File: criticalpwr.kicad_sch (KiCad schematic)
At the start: 6 parts, among them J3 Power Conn

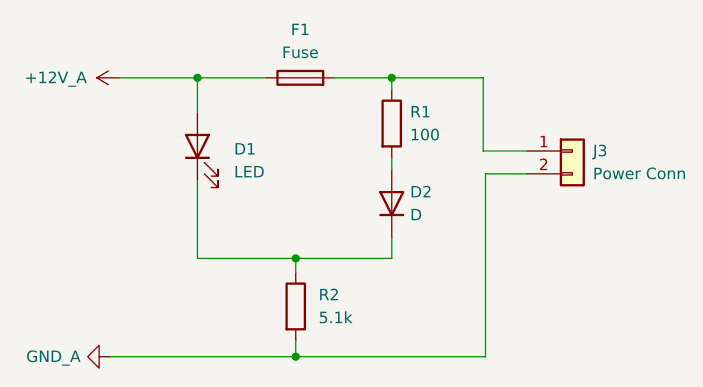
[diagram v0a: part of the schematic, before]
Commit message: removed LEDs
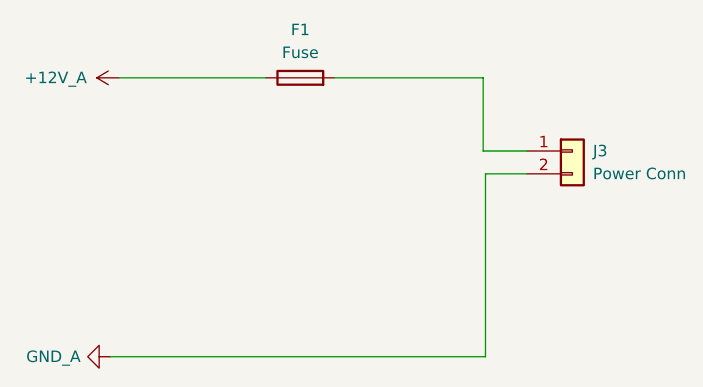
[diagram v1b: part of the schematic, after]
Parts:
- removed D1: LED, symbol Device:LED
- removed D2: D, symbol Device:D
- removed R1: 100, symbol Device:R
- removed R2: 5.1k, symbol Device:R

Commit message: finished schematic
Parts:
- added D1, D2, D20, D3, D4, D5, D6: 20mA, LED_SMD:LED_0805_2012Metric, symbol Device:LED
- added F22, F4, F5, F6, F7, F8: 10A, footprints:3588, symbol Device:Fuse
- added J10, J22, J6, J7, J8, J9: CRIT OUT, footprints:Molex_Micro-Fit_3.0_43650-0215_1x02_P3.00mm_Vertical, symbol Connector_Generic:Conn_01x02
- added R1, R2, R20, R3, R4, R5, R6: 505, Resistor_SMD:R_0805_2012Metric, symbol Device:R
- F1: value Fuse -> 10A
- J3: value Power Conn -> CRIT OUT
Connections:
- net at F1.2, J3.1 (Pin_1): now also R1.1
- net +12V_A renamed +12V_CRIT
- net +12V_CRIT: now also F22.1, F4.1, F5.1, F6.1, F7.1, F8.1
- net GND_A renamed GND
- net GND: now also D1.1 (K), D2.1 (K), D20.1 (K), D3.1 (K), D4.1 (K), D5.1 (K), D6.1 (K), J10.2 (Pin_2), J22.2 (Pin_2), J6.2 (Pin_2), J7.2 (Pin_2), J8.2 (Pin_2), J9.2 (Pin_2)
- new net: F5.2, J7.1 (Pin_1), R3.1
- new net: F4.2, J6.1 (Pin_1), R2.1
- new net: D6.2 (A), R6.2
- new net: F22.2, J22.1 (Pin_1), R20.1
- new net: D20.2 (A), R20.2
- new net: D1.2 (A), R1.2
- new net: F8.2, J10.1 (Pin_1), R6.1
- new net: D2.2 (A), R2.2
- new net: D4.2 (A), R4.2
- new net: F6.2, J8.1 (Pin_1), R4.1
- new net: F7.2, J9.1 (Pin_1), R5.1
- new net: D5.2 (A), R5.2
- new net: D3.2 (A), R3.2

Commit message: finished pcb
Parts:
- R1, R2, R20, R3, R4, R5, R6: value 505 -> 1k
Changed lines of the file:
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@@
 			)
 		)
-		(property "Value" "505"
+		(property "Value" "1k"
 			(at 58.42 32.766 90)
 			(effects
@@
 			)
 		)
-		(property "Value" "505"
+		(property "Value" "1k"
 			(at 119.38 94.996 90)
 			(effects
@@
 			)
 		)
-		(property "Value" "505"
+		(property "Value" "1k"
 			(at 58.42 94.996 90)
 			(effects
@@
 			)
 		)
-		(property "Value" "505"
+		(property "Value" "1k"
 			(at 119.38 32.766 90)
 			(effects
@@
 			)
 		)
-		(property "Value" "505"
+		(property "Value" "1k"
 			(at 58.42 63.246 90)
 			(effects
@@
 			)
 		)
-		(property "Value" "505"
+		(property "Value" "1k"
 			(at 119.38 63.246 90)
 			(effects
@@
 			)
 		)
-		(property "Value" "505"
+		(property "Value" "1k"
 			(at 58.42 128.016 90)
 			(effects

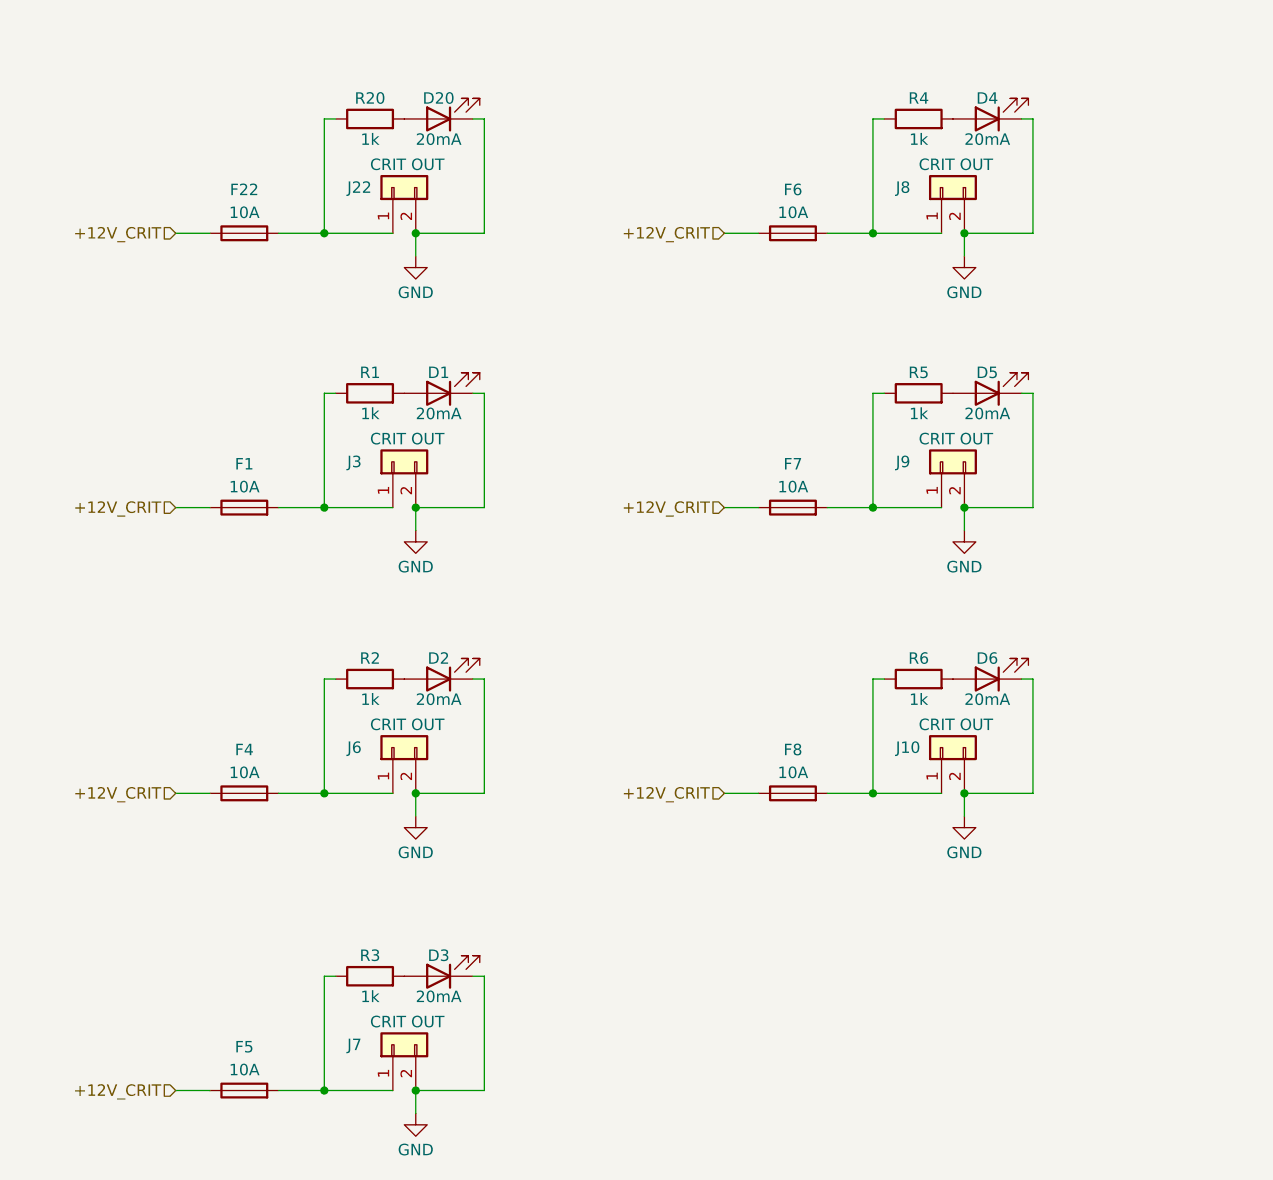
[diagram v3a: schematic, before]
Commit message: rearranged fuses on the back and and connectors on the front for improved waterproofing
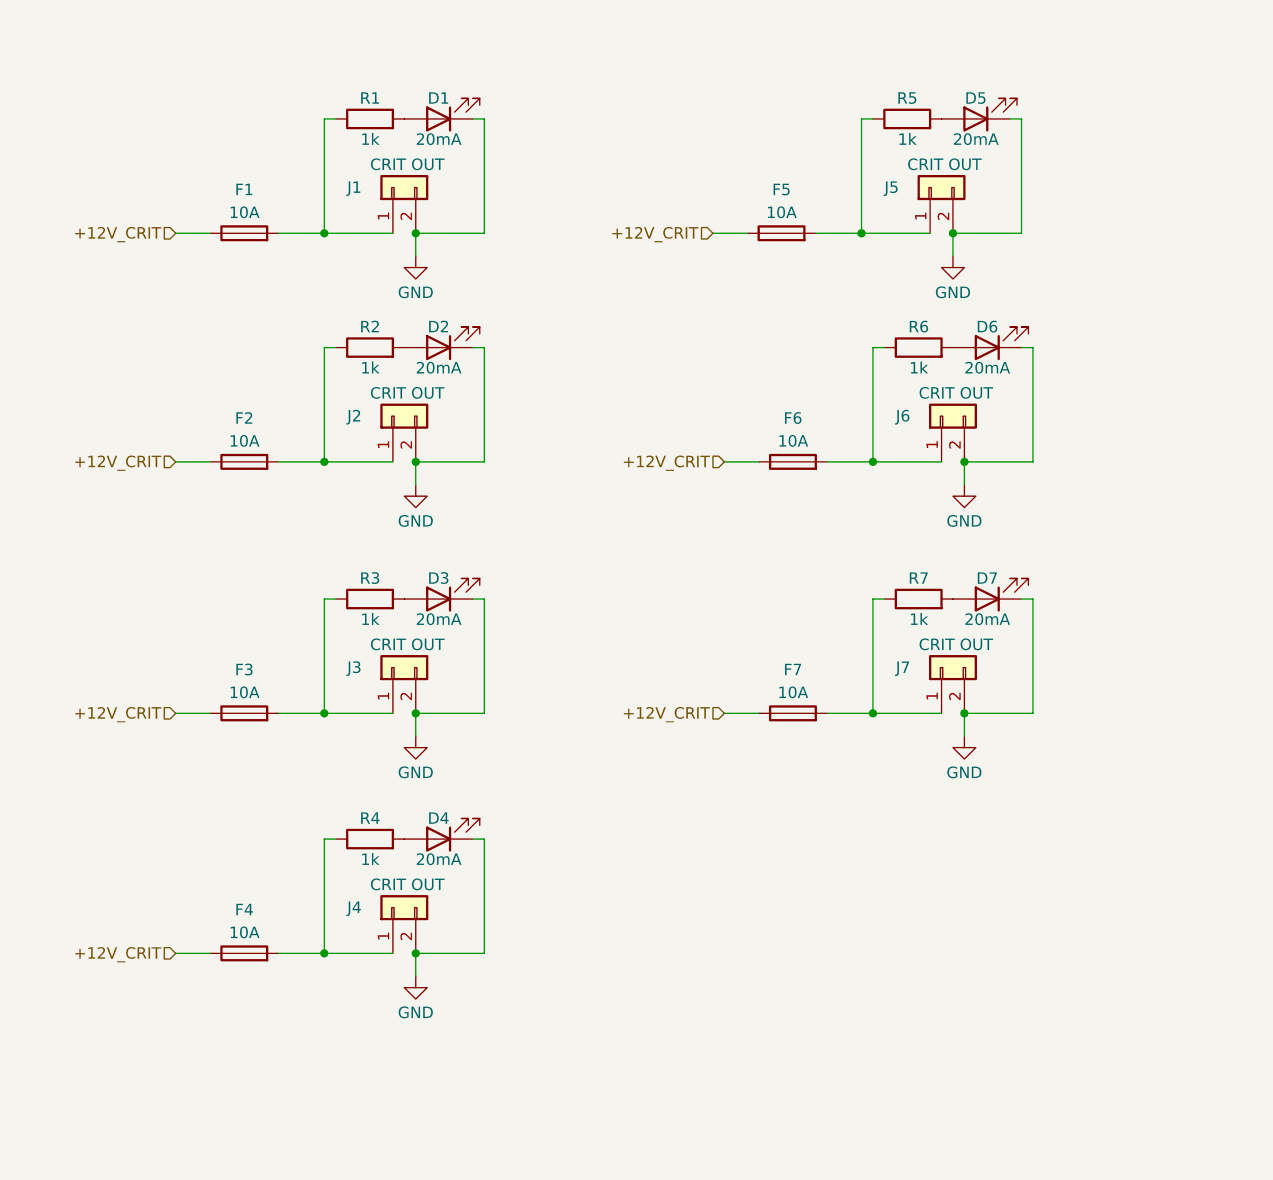
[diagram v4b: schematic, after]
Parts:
- renumbered D20 to D1, D6 to D2, D5 to D3, D3 to D5, D2 to D6, D1 to D7, F22 to F1, F8 to F2, F7 to F3, F6 to F4, F4 to F6, F1 to F7, J22 to J1, J10 to J2, J9 to J3, J8 to J4, J7 to J5, J3 to J7, R20 to R1, R6 to R2, R5 to R3, R3 to R5, R2 to R6, R1 to R7
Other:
- moved on the sheet: D2, D3, D4, D5, D6, D7, F2, F3, F4, F5, F6, F7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

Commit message: reoriented fuses horizontally to fit enclosure dimensions
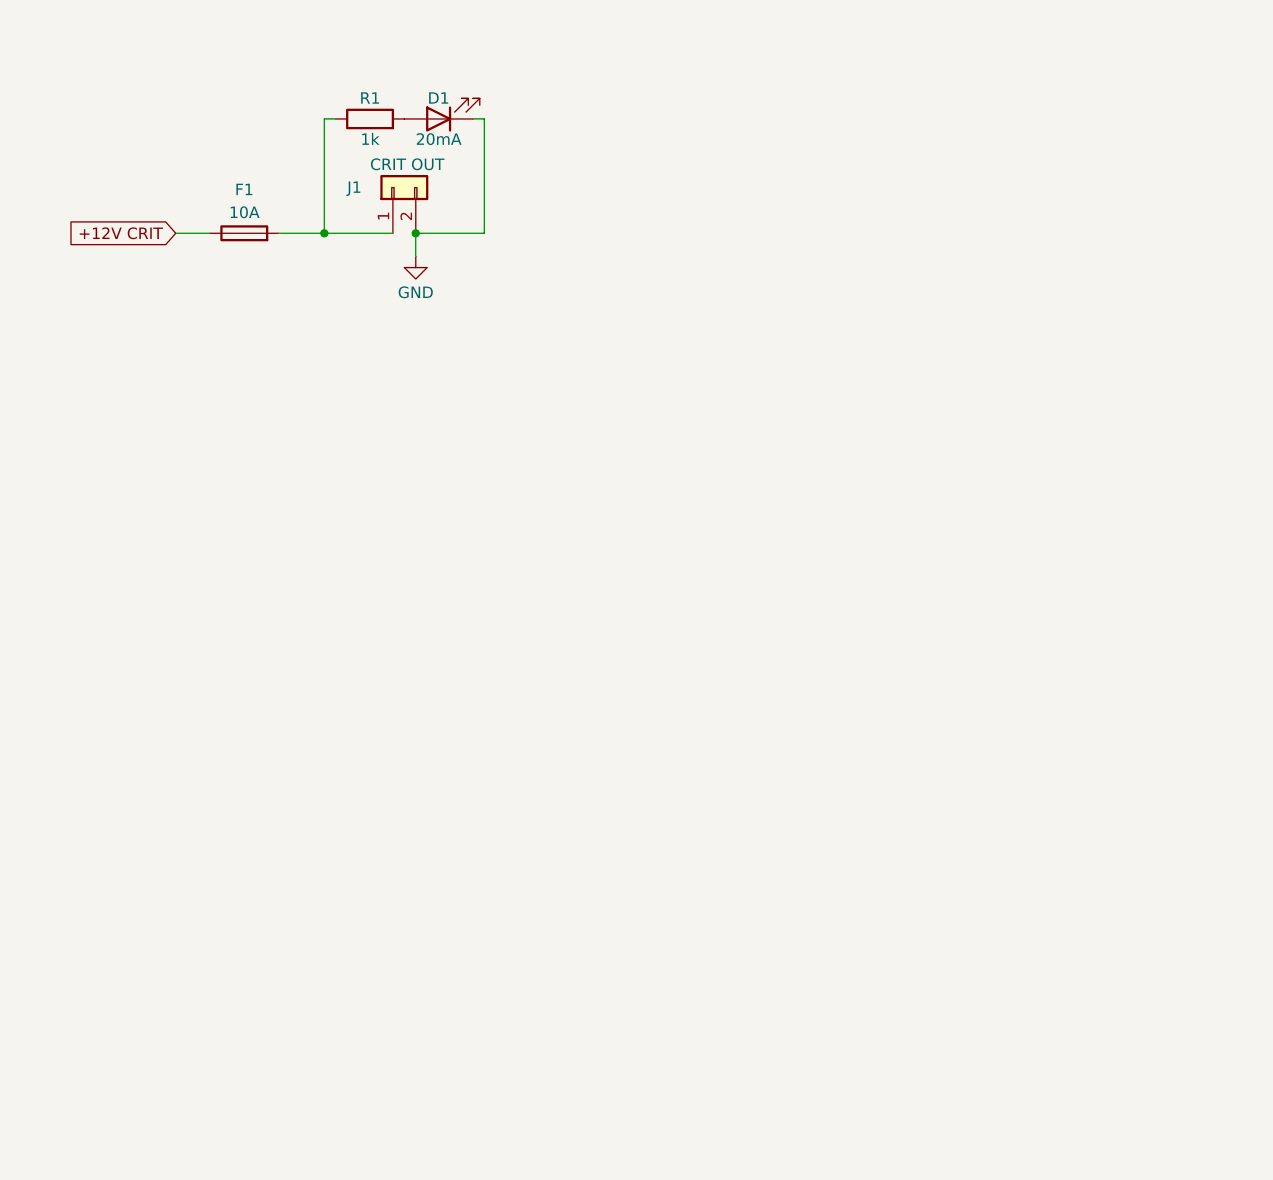
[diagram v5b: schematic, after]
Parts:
- removed D2, D3, D4, D5, D6, D7: 20mA, LED_SMD:LED_0805_2012Metric, symbol Device:LED
- removed F2, F3, F4, F5, F6, F7: 10A, footprints:3588, symbol Device:Fuse
- removed J2, J3, J4, J5, J6, J7: CRIT OUT, footprints:Molex_Micro-Fit_3.0_43650-0215_1x02_P3.00mm_Vertical, symbol Connector_Generic:Conn_01x02
- removed R2, R3, R4, R5, R6, R7: 1k, Resistor_SMD:R_0805_2012Metric, symbol Device:R
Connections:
- net +12V_CRIT renamed +12V CRIT

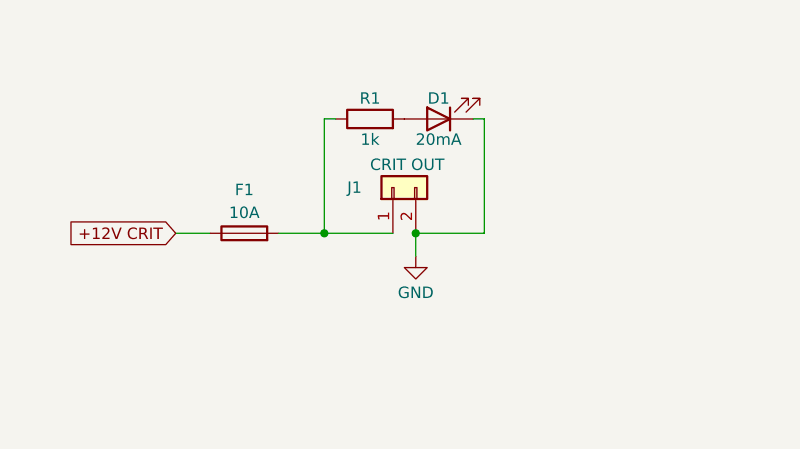
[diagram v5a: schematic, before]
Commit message: Added optoisolators to ensure LED indicators are powered by critical power and only turn on when the fuse blows. Fuses and resistors on the back for waterproofing.
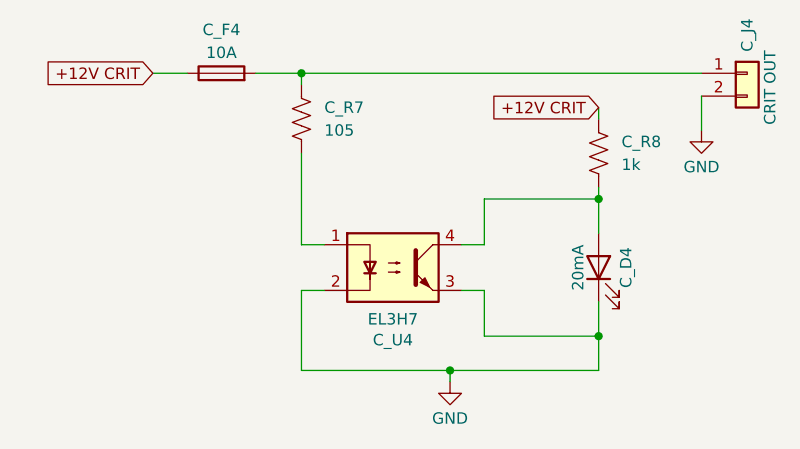
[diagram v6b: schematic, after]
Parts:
- removed D1: 20mA, LED_SMD:LED_0805_2012Metric, symbol Device:LED
- removed F1: 10A, footprints:3588, symbol Device:Fuse
- removed J1: CRIT OUT, footprints:Molex_Micro-Fit_3.0_43650-0215_1x02_P3.00mm_Vertical, symbol Connector_Generic:Conn_01x02
- removed R1: 1k, Resistor_SMD:R_0805_2012Metric, symbol Device:R
- added C_D4: 20mA, LED_SMD:LED_0805_2012Metric, symbol Device:LED
- added C_F4: 10A, footprints:3588, symbol Device:Fuse
- added C_J4: CRIT OUT, footprints:Molex_Micro-Fit_3.0_43650-0215_1x02_P3.00mm_Vertical, symbol Connector_Generic:Conn_01x02
- added C_R7: 105, Resistor_SMD:R_0805_2012Metric, symbol Device:R_US
- added C_R8: 1k, Resistor_SMD:R_0805_2012Metric, symbol Device:R_US
- added C_U4: EL3H7, Package_SO:SOP-4_4.4x2.6mm_P1.27mm, symbol Isolator:SFH617A-1
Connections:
- net +12V CRIT: now also C_F4.1, C_R8.1
- net GND: now also C_D4.1 (K), C_J4.2 (Pin_2), C_U4.2, C_U4.3
- new net: C_F4.2, C_J4.1 (Pin_1), C_R7.1
- new net: C_R7.2, C_U4.1
- new net: C_D4.2 (A), C_R8.2, C_U4.4

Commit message: solder bridges
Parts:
- added JP32: SolderJumper_2_Open, Jumper:SolderJumper-2_P1.3mm_Open_TrianglePad1.0x1.5mm, symbol Jumper:SolderJumper_2_Open
- renumbered C_D4 to C_D1, C_F4 to C_F1, C_J4 to C_J1, C_R7 to C_R1, C_R8 to C_R2, C_U4 to C_U1
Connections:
- net at C_R1.2: now also JP32.1 (A); no longer C_U1.1
- new net: C_U1.1, JP32.2 (B)
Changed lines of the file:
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@@
 (kicad_sch
-	(version 20231120)
+	(version 20250114)
 	(generator "eeschema")
-	(generator_version "8.0")
+	(generator_version "9.0")
 	(paper "A4")
 	(junction
@@
 	(wire
 		(pts
+			(xy 50.8 43.18) (xy 50.8 44.45)
+		)
+		(stroke
+			(width 0)
+			(type default)
+		)
+	)
+	(wire
+		(pts
 			(xy 71.12 49.53) (xy 68.58 49.53)
 		)
@@
 	(wire
 		(pts
-			(xy 50.8 34.29) (xy 50.8 44.45)
+			(xy 50.8 34.29) (xy 50.8 35.56)
 		)
 		(stroke
@@
 		(dnp no)
 		(fields_autoplaced yes)
-		(property "Reference" "C_R7"
+		(property "Reference" "C_R1"
 			(at 53.34 29.2099 0)
 			(effects
@@
 		(on_board yes)
 		(dnp no)
-		(property "Reference" "C_U4"
+		(property "Reference" "C_U1"
 			(at 60.96 55.0418 0)
 			(effects
@@
 		(on_board yes)
 		(dnp no)
-		(property "Reference" "C_D4"
+		(property "Reference" "C_D1"
 			(at 86.868 46.99 0)
 			(effects
@@
 		(on_board yes)
 		(dnp no)
-		(property "Reference" "C_J4"
+		(property "Reference" "C_J1"
 			(at 100.33 19.304 90)
 			(effects
@@
 		(on_board yes)
 		(dnp no)
-		(property "Reference" "#PWR031"
+		(property "Reference" "#PWR027"
 			(at 95.25 38.1 0)
 			(effects
@@
 		(on_board yes)
 		(dnp no)
-		(property "Reference" "C_F4"
+		(property "Reference" "C_F1"
 			(at 41.91 20.574 90)
 			(effects
@@
 		(dnp no)
 		(fields_autoplaced yes)
-		(property "Reference" "C_R8"
+		(property "Reference" "C_R2"
 			(at 86.36 33.0199 0)
 			(effects
@@
 		(on_board yes)
 		(dnp no)
-		(property "Reference" "#PWR023"
+		(property "Reference" "#PWR020"
 			(at 67.31 66.04 0)
 			(effects
@@
 					(unit 1)
 				)
+			)
+		)
+	)
+	(symbol
+		(lib_id "Jumper:SolderJumper_2_Open")
+		(at 50.8 39.37 270)
+		(unit 1)
+		(exclude_from_sim no)
+		(in_bom no)
+		(on_board yes)
+		(dnp no)
+		(property "Reference" "JP32"
+			(at 48.006 38.354 90)
+			(effects
+				(font
+					(size 1.27 1.27)
+				)
+				(justify right)
+			)
+		)
+		(property "Value" "SolderJumper_2_Open"
+			(at 48.006 40.64 90)
+			(effects
+				(font
+					(size 1.27 1.27)
+				)
+				(justify right)
+			)
+		)
+		(property "Footprint" "Jumper:SolderJumper-2_P1.3mm_Open_TrianglePad1.0x1.5mm"
+			(at 50.8 39.37 0)
+			(effects
+				(font
+					(size 1.27 1.27)
+				)
+				(hide yes)
+			)
+		)
+		(property "Datasheet" "~"
+			(at 50.8 39.37 0)
+			(effects
+				(font
+					(size 1.27 1.27)
+				)
+				(hide yes)
+			)
+		)
+		(property "Description" "Solder Jumper, 2-pole, open"
+			(at 50.8 39.37 0)
+			(effects
+				(font
+					(size 1.27 1.27)
+				)
+				(hide yes)
+			)
+		)
+		(pin "2"
+		)
+		(pin "1"
+		)
+		(instances
+			(project "PS-LVDistributionPCB"
+				(path "/bae4e46c-28ae-4193-a5e0-928c081802f5/0e93146d-5ace-49a5-b60a-5dbdc2be7e21"
+					(reference "JP35")
+					(unit 1)
+				)
+				(path "/bae4e46c-28ae-4193-a5e0-928c081802f5/396ce50b-4b4c-4dff-8b81-60ffdff640fe"
+					(reference "JP36")
+					(unit 1)
+				)
+				(path "/bae4e46c-28ae-4193-a5e0-928c081802f5/3d343d5f-ea66-42dd-b89e-d8730c226c48"
+					(reference "JP37")
+					(unit 1)
+				)
+				(path "/bae4e46c-28ae-4193-a5e0-928c081802f5/4111fdfe-1fcc-4bb2-9192-3f2c5d7f36cc"
+					(reference "JP34")
+					(unit 1)
+				)
+				(path "/bae4e46c-28ae-4193-a5e0-928c081802f5/82d3b830-d39d-4669-a583-e3cf5f4df988"
+					(reference "JP38")
+					(unit 1)
+				)
+				(path "/bae4e46c-28ae-4193-a5e0-928c081802f5/89225460-8dd3-469b-8cbf-e885cf1901f0"
+					(reference "JP32")
+					(unit 1)
+				)
+				(path "/bae4e46c-28ae-4193-a5e0-928c081802f5/b72bae1b-f8fb-497f-abbd-36694efca097"
+					(reference "JP33")
+					(unit 1)
+				)
